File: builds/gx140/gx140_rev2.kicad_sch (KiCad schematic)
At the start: 14 parts

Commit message: Replace old GX140 drawings and PDFs with rev2 KiCad schematic
Co-Authored-By: Claude Sonnet 4.6 (1M context) <noreply@anthropic.com>
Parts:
- removed ? (x3): (no value), symbol grok:ANT
- removed ? (x4): (no value), symbol grok:MOTOR
- removed ?: (no value), symbol grok:RX
- removed ?: (no value), symbol grok:FC
- removed ?: (no value), symbol grok:VTX
- removed ?: (no value), symbol grok:BAT
- removed ?: (no value), symbol grok:ESC
- removed ?: (no value), symbol grok:GPS
- removed ?: (no value), symbol grok:CAM
- added AE1: SMA_Foxeer_Lollipop_RHCP, symbol grok:ANTENNA
- added AE2: ANT1_vert_L_standoff, symbol grok:ANTENNA
- added AE3: ANT2_horiz_top_plate, symbol grok:ANTENNA
- added BAT1: 2S_550mAh_LiHV_XT30, symbol grok:BATTERY_2S
- added CAM1: Caddx_Ant_1200TVL, symbol grok:CAM_CADDX_ANT
- added ESC1: BLS_35A_4in1_20x20_DShot600, symbol grok:ESC_BLS35A_4IN1
- added FC1: SpeedyBee_F405_Mini_20x20, symbol grok:FC_F405_MINI
- added GPS1: Matek_M10Q-5883_(opt), symbol grok:GPS_M10Q_5883
- added M1: Specter_1804_FL_CCW, symbol grok:MOTOR_1804
- added M2: Specter_1804_FR_CW, symbol grok:MOTOR_1804
- added M3: Specter_1804_RL_CCW, symbol grok:MOTOR_1804
- added M4: Specter_1804_RR_CW, symbol grok:MOTOR_1804
- added RX1: BETAFPV_SuperD_ELRS_Diversity, symbol grok:RX_SUPERD_ELRS
- added VTX1: HGLRC_Zeus_350mW_SmartAudio, symbol grok:VTX_ZEUS350
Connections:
- net 5V: now also CAM1.1 (5V), FC1.8 (5V), GPS1.1 (5V), RX1.1 (5V), VTX1.1 (5V)
- net CAM_VIDEO: now also CAM1.3 (VID), FC1.9 (VIN)
- net DSHOT_M1: now also ESC1.3 (S1), FC1.4 (M1)
- net DSHOT_M2: now also ESC1.4 (S2), FC1.5 (M2)
- net DSHOT_M3: now also ESC1.5 (S3), FC1.6 (M3)
- net DSHOT_M4: now also ESC1.6 (S4), FC1.7 (M4)
- net I2C_SCL: now also FC1.18 (SCL), GPS1.6 (SCL)
- net I2C_SDA: now also FC1.17 (SDA), GPS1.5 (SDA)
- net M1_A: now also ESC1.8 (M1_A), M1.1 (A)
- net M1_C: now also ESC1.10 (M1_C), M1.3 (C)
- net M2_A: now also ESC1.11 (M2_A), M2.1 (A)
- net M2_C: now also ESC1.13 (M2_C), M2.3 (C)
- net M3_A: now also ESC1.14 (M3_A), M3.1 (A)
- net M3_C: now also ESC1.16 (M3_C), M3.3 (C)
- net M4_A: now also ESC1.17 (M4_A), M4.1 (A)
- net M4_B: now also ESC1.18 (M4_B), M4.2 (B)
- net M4_C: now also ESC1.19 (M4_C), M4.3 (C)
- net RX_ANT1: now also AE2.1 (FEED), RX1.5 (ANT1)
- net RX_ANT2: now also AE3.1 (FEED), RX1.6 (ANT2)
- net VBAT: now also BAT1.1 (VBAT+), ESC1.1 (VBAT+), FC1.1 (VBAT)
- net VTX_ANT: now also AE1.1 (FEED), VTX1.5 (ANT)
- new net ESC_CURR: ESC1.7 (CURR), FC1.3 (CURR)
- new net GND: BAT1.2 (VBAT-), CAM1.2 (GND), ESC1.2 (VBAT-), FC1.2 (GND), GPS1.2 (GND), RX1.2 (GND), VTX1.2 (GND)
- new net M1_B: ESC1.9 (M1_B), M1.2 (B)
- new net M2_B: ESC1.12 (M2_B), M2.2 (B)
- new net M3_B: ESC1.15 (M3_B), M3.2 (B)
- new net RX3_GPS: FC1.16 (RX3), GPS1.4 (TX)
- new net RX5_CRSF: FC1.14 (RX5), RX1.4 (TX)
- new net TX3_GPS: FC1.15 (TX3), GPS1.3 (RX)
- new net TX4_SMARTAUDIO: FC1.11 (TX4), VTX1.4 (SA)
- new net TX5_CRSF: FC1.13 (TX5), RX1.3 (RX)
- new net VTX_VIDEO: FC1.10 (VOUT), VTX1.3 (VID_IN)
- no-connect marks 0 -> 1
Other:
- note added: "22AWG: VBAT, GND, motor phase | 26AWG: UART, DShot, video | 28AWG: I2C"
- note added: "=== UART MAP (F405 Mini) ==="
- note added: "=== VIDEO PATH (corrected) ==="
- note added: "=== WIRING ==="
- note added: "BAT XT30 -> ESC VBAT pads (22AWG). FC powered via ESC 8-pin harness (VBAT/GND/CURR/S1-S4)."
- note added: "CAM.VID -> FC.VIN (CAM_VIDEO) -> AT7456E OSD -> FC.VOUT -> VTX.VID_IN (VTX_VIDEO)."
- note added: "Continuity check VBAT-GND before battery | Verify motor order/direction in Betaflight Motors tab"
- note added: "FC internal 5V/3A BEC -> 5V net -> VTX, CAM, RX, GPS."
- note added: "GX140 3in ANALOG FPV — ELECTRICAL SCHEMATIC (Rev 2.0)"
- note added: "Grok rev1 bypassed the OSD: camera direct to VTX = no Betaflight OSD overlay."
- note added: "JST-SH 1.0mm: CAM | JST-GH 1.25mm: GPS | XT30: battery | Heat shrink all joints"
- note added: "METHOD: point-to-point by net label. Every conductor breaks out at the device pin."
- note added: "MOTOR PHASE WIRING: 3 conductors per motor (A/B/C)."
- note added: "Match net names to find the far end. No routed runs, no crossings, no junction ambiguity."
- note added: "Smoke stopper (ShortSaver) MANDATORY first power-up | Props OFF for motor direction test"
- note added: "Swap any two phases to reverse direction. M1 FL CCW | M2 FR CW | M3 RL CCW | M4 RR CW."
- note added: "UART3: GPS 57600 (TX3_GPS / RX3_GPS) | UART4: SmartAudio 2.1 (TX4 only, RX4 = N/C)"
- note added: "UART5: ELRS CRSF 420k (TX5_CRSF -> RX.RX, RX.TX -> RX5_CRSF) | I2C: QMC5883L compass"
- note removed: "2S 550mAh LiHV (7.4V) XT30 → FC VBAT → Internal 5V/3A BEC → 5V Rail"
- note removed: "2S 550mAh LiHV 7.4V XT30"
- note removed: "5V Rail powers: VTX, CAM, RX, GPS (optional)"
- note removed: "5V: FC1.5V → VTX1.5V → CAM1.5V → RX1.5V → GPS1.5V"
- note removed: "=== BUILD SPECS ==="
- note removed: "=== NET CROSS-REFERENCE ==="
- note removed: "=== SIGNAL SUMMARY ==="
- note removed: "BAT1"
- note removed: "BAT: 2S 550mAh LiHV 7.6V 75C XT30 30×18×15mm ~4-5min LVC 3.5V/cell"
- note removed: "BETAFPV SuperD ELRS V3 22x14mm Dual SX1280"
- note removed: "BLS 35A 4in1 20x20 DShot600 3-6S"
- note removed: "CAM Video → VTX CAM_IN (JST-SH 1.0mm 4-pin)"
- note removed: "CAM1"
- note removed: "CAM: Caddx Ant 1200TVL 14×14→19×19 adapter F1.6 165° JST-SH 1.0mm 4-pin"
- note removed: "CAM_VIDEO: CAM1.CAM_VIDEO → VTX1.CAM_VIDEO (JST-SH 1.0mm)"
- note removed: "CURR: ESC1.CURR → FC1.CURR (current sense, if supported)"
- note removed: "Caddx Ant 1200TVL 14x14→19x19 F1.6 JST-SH"
- note removed: "Continuity check all rails | AUW ~190g (<250g) | CG <1mm | ALL DIRECT FIT"
- note removed: "DSHOT_M1-M4: FC1.M1-M4 → ESC1.DSHOT_M1-M4 (DShot600)"
- note removed: "DShot600: FC M1-M4 → ESC → Motors (bidirectional, RPM filter ON)"
- note removed: "ESC1"
- note removed: "ESC: BLS 35A 4in1 20×20 DShot600 Bidir ON | 25×25×4.5mm | 3-6S | 5V/3A BEC"
- note removed: "FC1"
- note removed: "FC: SpeedyBee F405 Mini 20×20 ICM42688 DPS310 | 25×25×6.5mm | 4 UARTs USB-C"
- note removed: "Frame: GX140 140mm 4mm CF twin 20x20 | 8× M3×25mm alu standoffs | ~45g bare"
- note removed: "GND: BAT1.GND → ESC1.GND → FC1.GND → VTX1.GND → CAM1.GND → RX1.GND → GPS1.GND"
- note removed: "GPS1"
- note removed: "GPS: Matek M10Q-5883 UBLOX M10 QMC5883L (optional) JST-GH 1.25mm 6-pin"
- note removed: "GROK — FPV Drone Engineering | 2025-12-12 | Rev 2.0 | Sheet 1/1 | A3"
- note removed: "GX140 3in ANALOG FPV — Electrical Schematic"
- note removed: "HGLRC Specter 1804 3500KV M1 FL CCW"
- note removed: "HGLRC Specter 1804 3500KV M2 FR CW"
- note removed: "HGLRC Specter 1804 3500KV M3 RL CCW"
- note removed: "HGLRC Specter 1804 3500KV M4 RR CW"
- note removed: "HGLRC Zeus 350mW 16x16→20x20 SmartAudio"
- note removed: "I2C_SDA/SCL: FC1.I2C → GPS1.I2C (QMC5883L compass)"
- note removed: "M1"
- note removed: "M1_A-M4_C: ESC1.M1_A-M4_C → M1-M4 (Motor phases)"
- note removed: "M2"
- note removed: "M3"
- note removed: "M4"
- note removed: "Matek M10Q-5883 UBLOX M10 QMC5883L (optional)"
- note removed: "Motors: HGLRC Specter 1804 3500KV 13.3g 12×12 M2 1.5mm shaft 22.68×13.2mm"
- note removed: "Props: GEMFAN 3052 3in tri-blade 5mm hub+1.5mm adapter 22.8mm tip clearance"
- note removed: "RX1"
- note removed: "RX3/TX3: FC1.RX3 → GPS1.TX3 | FC1.TX3 → GPS1.RX3 (UBLOX)"
- note removed: "RX: BETAFPV SuperD ELRS 22×14mm 1.1g Dual SX1280 CRSF@420k ANT1 vert L ANT2 horiz"
- note removed: "SMA → Foxeer Lollipop RHCP"
- note removed: "ShortSaver MANDATORY before first power | Props OFF for motor direction test"
- note removed: "SpeedyBee F405 Mini 20x20 ICM42688 DPS310 4 UARTs"
- note removed: "TX4: FC1.TX4 → VTX1.TX4 (SmartAudio PA control)"
- note removed: "TX5/RX5: FC1.TX5 → RX1.RX5 | RX1.TX5 → FC1.RX5 (CRSF)"
- note removed: "UART3 (TX3/RX3): FC ↔ GPS UBLOX — M10Q-5883, 57600 baud (optional)"
- note removed: "UART4 (TX4): FC → VTX SmartAudio RX — PA control, 115200 baud"
- note removed: "UART5 (TX5/RX5): FC ↔ RX CRSF — ELRS V3, 420000 baud"
- note removed: "VBAT: BAT1.VBAT → ESC1.VBAT → FC1.VBAT"
- note removed: "VTX1"
- note removed: "VTX: HGLRC Zeus 350mW 16×16→20×20 SmartAudio SMA Foxeer Lollipop RHCP"
- company: GROK — FPV Drone Engineering -> GX140 Build — net-label point-to-point method

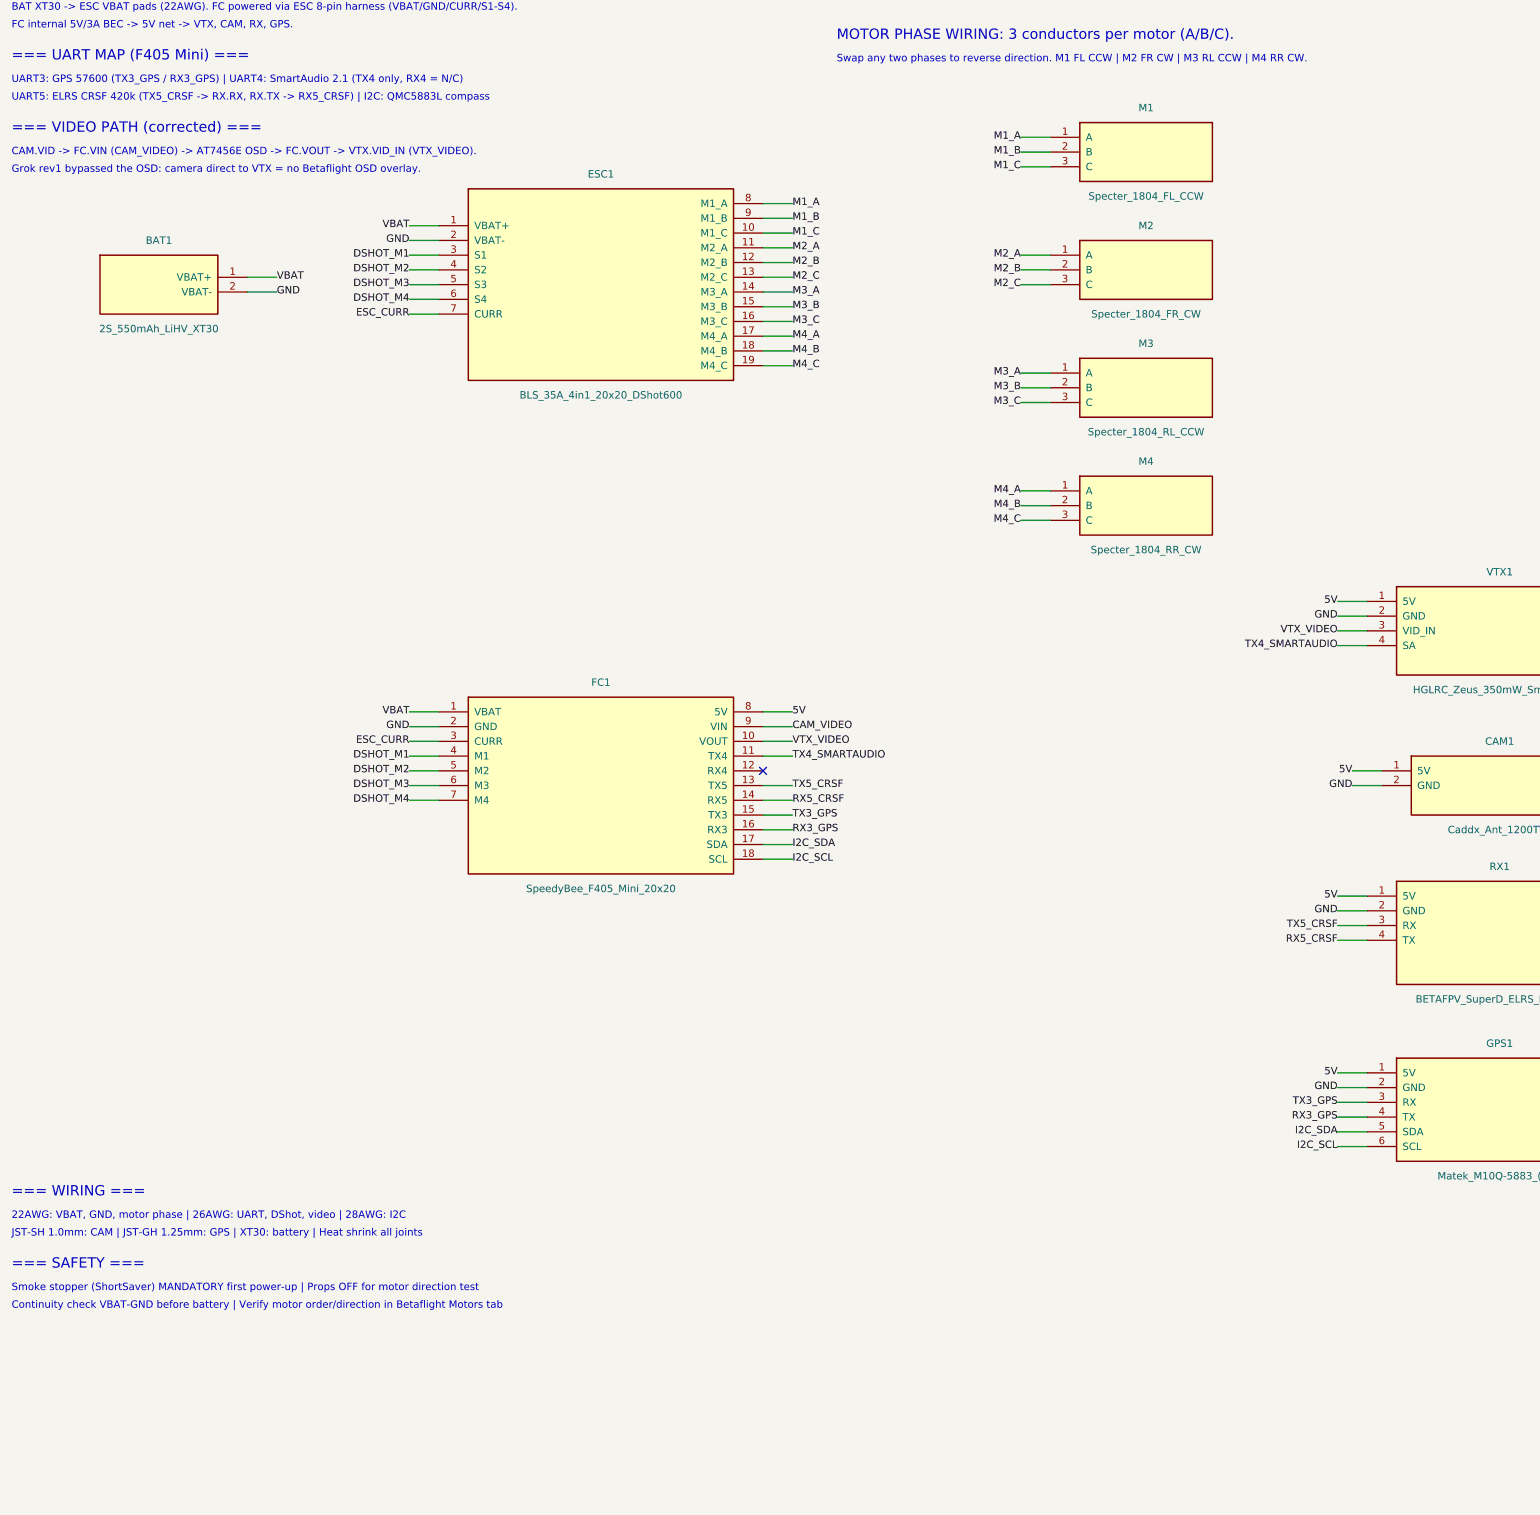
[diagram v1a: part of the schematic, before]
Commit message: Add engineering package text annotations to KiCad schematic
Full wire schedule, reverse wire tagging method, stack assembly
layers, torque specs, mounting notes, antenna layout, battery
info, and Betaflight config — all in-schematic annotations.

Co-Authored-By: Claude Sonnet 4.6 (1M context) <noreply@anthropic.com>
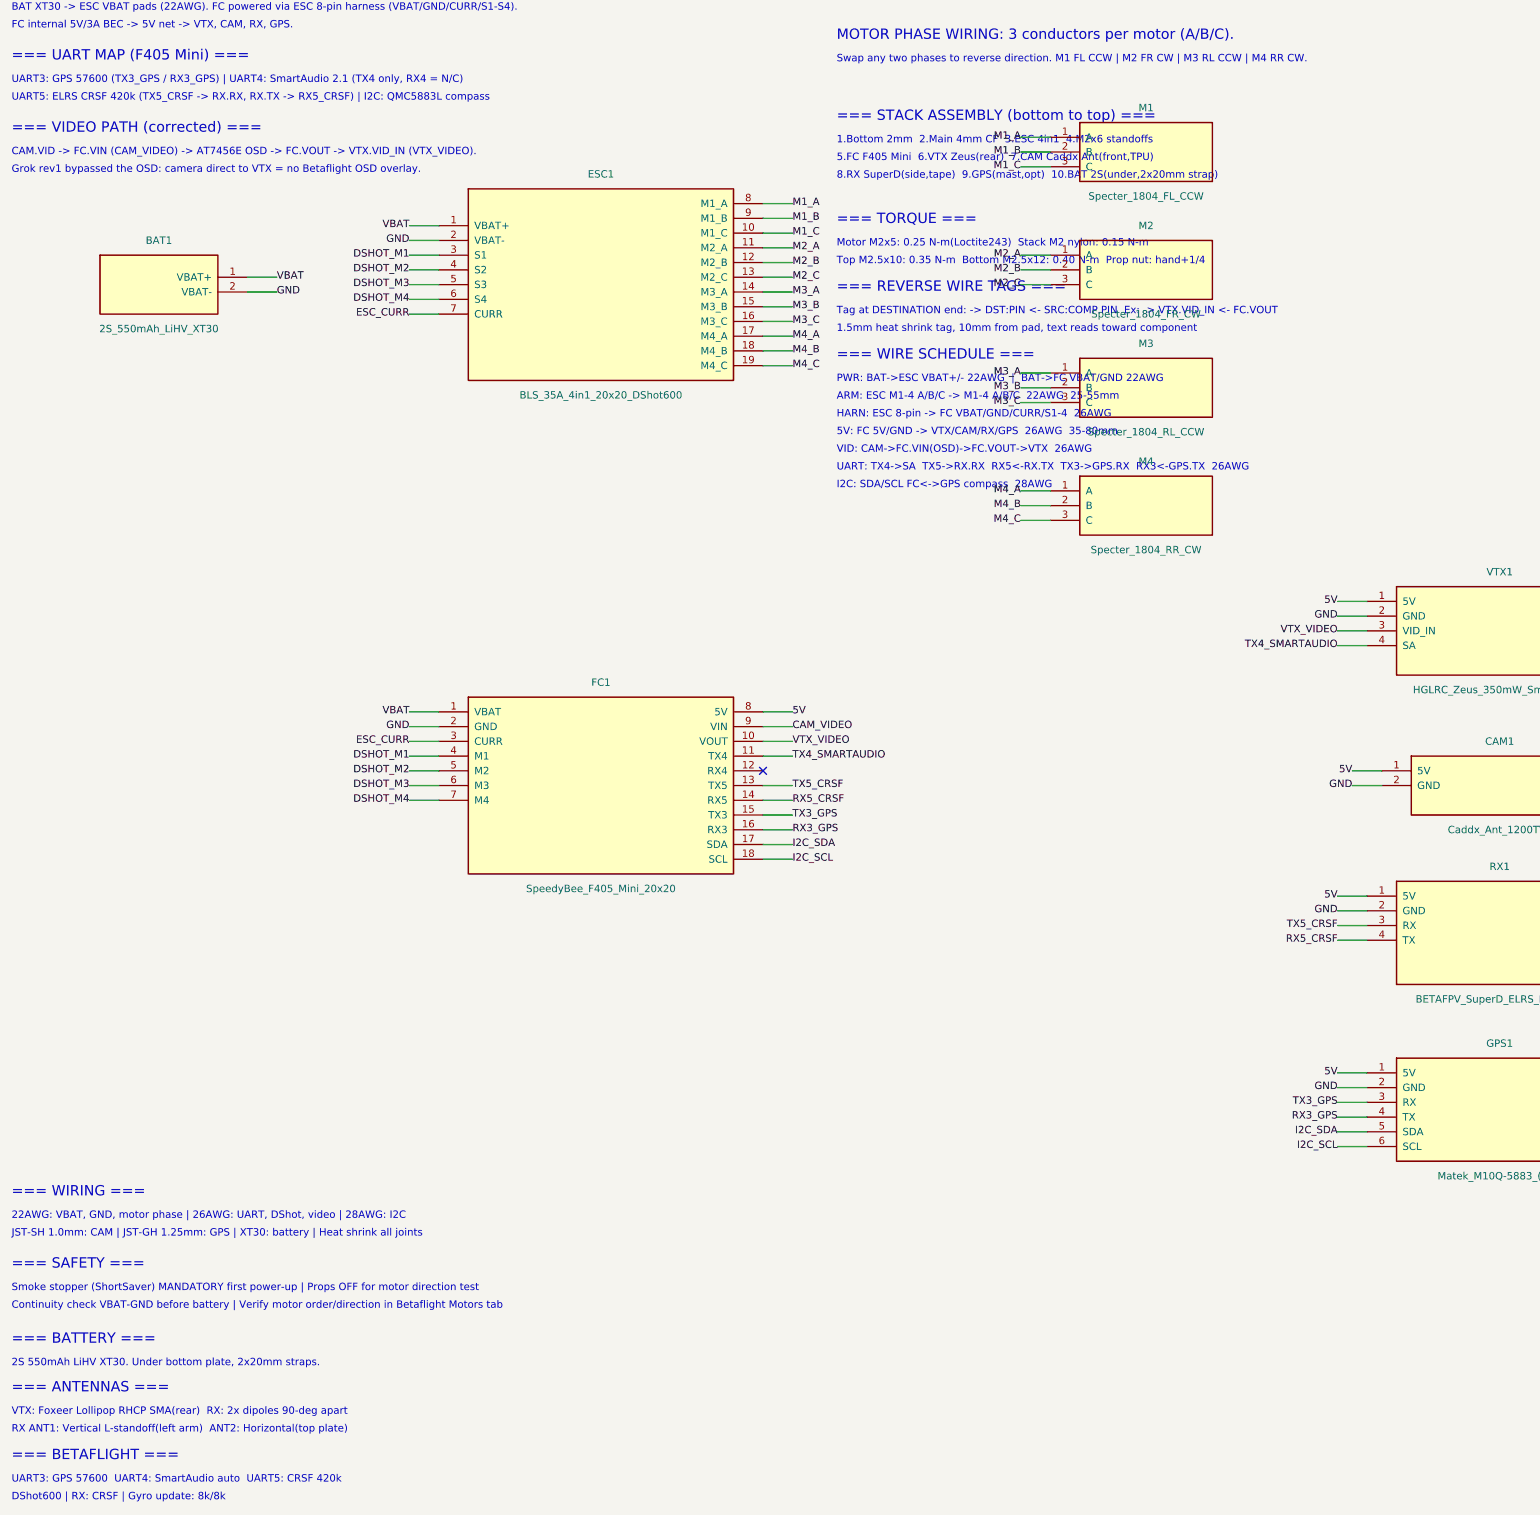
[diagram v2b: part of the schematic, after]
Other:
- note added: "1.5mm heat shrink tag, 10mm from pad, text reads toward component"
- note added: "1.Bottom 2mm 2.Main 4mm CF 3.ESC 4in1 4.M2x6 standoffs"
- note added: "2S 550mAh LiHV XT30. Under bottom plate, 2x20mm straps."
- note added: "5.FC F405 Mini 6.VTX Zeus(rear) 7.CAM Caddx Ant(front,TPU)"
- note added: "5V: FC 5V/GND -> VTX/CAM/RX/GPS 26AWG 35-80mm"
- note added: "8.RX SuperD(side,tape) 9.GPS(mast,opt) 10.BAT 2S(under,2x20mm strap)"
- note added: "=== ANTENNAS ==="
- note added: "=== BATTERY ==="
- note added: "=== BETAFLIGHT ==="
- note added: "=== REVERSE WIRE TAGS ==="
- note added: "=== STACK ASSEMBLY (bottom to top) ==="
- note added: "=== TORQUE ==="
- note added: "=== WIRE SCHEDULE ==="
- note added: "ARM: ESC M1-4 A/B/C -> M1-4 A/B/C 22AWG 25-55mm"
- note added: "DShot600 | RX: CRSF | Gyro update: 8k/8k"
- note added: "HARN: ESC 8-pin -> FC VBAT/GND/CURR/S1-4 26AWG"
- note added: "I2C: SDA/SCL FC<->GPS compass 28AWG"
- note added: "Motor M2x5: 0.25 N-m(Loctite243) Stack M2 nylon: 0.15 N-m"
- note added: "PWR: BAT->ESC VBAT+/- 22AWG | BAT->FC VBAT/GND 22AWG"
- note added: "RX ANT1: Vertical L-standoff(left arm) ANT2: Horizontal(top plate)"
- note added: "Tag at DESTINATION end: -> DST:PIN <- SRC:COMP.PIN Ex: -> VTX.VID_IN <- FC.VOUT"
- note added: "Top M2.5x10: 0.35 N-m Bottom M2.5x12: 0.40 N-m Prop nut: hand+1/4"
- note added: "UART3: GPS 57600 UART4: SmartAudio auto UART5: CRSF 420k"
- note added: "UART: TX4->SA TX5->RX.RX RX5<-RX.TX TX3->GPS.RX RX3<-GPS.TX 26AWG"
- note added: "VID: CAM->FC.VIN(OSD)->FC.VOUT->VTX 26AWG"
- note added: "VTX: Foxeer Lollipop RHCP SMA(rear) RX: 2x dipoles 90-deg apart"
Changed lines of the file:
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@@
+    (effects (font (size 1.27 1.27)) (justify left bottom))
+  )
+  (text "=== STACK ASSEMBLY (bottom to top) ===" (at 167.64 60.96 0)
+    (effects (font (size 1.778 1.778)) (justify left bottom))
+  )
+  (text "1.Bottom 2mm  2.Main 4mm CF  3.ESC 4in1  4.M2x6 standoffs" (at 167.64 64.77 0)
+    (effects (font (size 1.27 1.27)) (justify left bottom))
+  )
+  (text "5.FC F405 Mini  6.VTX Zeus(rear)  7.CAM Caddx Ant(front,TPU)" (at 167.64 67.82 0)
+    (effects (font (size 1.27 1.27)) (justify left bottom))
+  )
+  (text "8.RX SuperD(side,tape)  9.GPS(mast,opt)  10.BAT 2S(under,2x20mm strap)" (at 167.64 70.87 0)
+    (effects (font (size 1.27 1.27)) (justify left bottom))
+  )
+  (text "=== TORQUE ===" (at 167.64 78.74 0)
+    (effects (font (size 1.778 1.778)) (justify left bottom))
+  )
+  (text "Motor M2x5: 0.25 N-m(Loctite243)  Stack M2 nylon: 0.15 N-m" (at 167.64 82.55 0)
+    (effects (font (size 1.27 1.27)) (justify left bottom))
+  )
+  (text "Top M2.5x10: 0.35 N-m  Bottom M2.5x12: 0.40 N-m  Prop nut: hand+1/4" (at 167.64 85.6 0)
+    (effects (font (size 1.27 1.27)) (justify left bottom))
+  )
+  (text "=== REVERSE WIRE TAGS ===" (at 167.64 90.42 0)
+    (effects (font (size 1.778 1.778)) (justify left bottom))
+  )
+  (text "Tag at DESTINATION end: -> DST:PIN <- SRC:COMP.PIN  Ex: -> VTX.VID_IN <- FC.VOUT" (at 167.64 94.23 0)
+    (effects (font (size 1.27 1.27)) (justify left bottom))
+  )
+  (text "1.5mm heat shrink tag, 10mm from pad, text reads toward component" (at 167.64 97.28 0)
+    (effects (font (size 1.27 1.27)) (justify left bottom))
+  )
+  (text "=== WIRE SCHEDULE ===" (at 167.64 102.11 0)
+    (effects (font (size 1.778 1.778)) (justify left bottom))
+  )
+  (text "PWR: BAT->ESC VBAT+/- 22AWG  |  BAT->FC VBAT/GND 22AWG" (at 167.64 105.92 0)
+    (effects (font (size 1.27 1.27)) (justify left bottom))
+  )
+  (text "ARM: ESC M1-4 A/B/C -> M1-4 A/B/C  22AWG  25-55mm" (at 167.64 108.97 0)
+    (effects (font (size 1.27 1.27)) (justify left bottom))
+  )
+  (text "HARN: ESC 8-pin -> FC VBAT/GND/CURR/S1-4  26AWG" (at 167.64 112.02 0)
+    (effects (font (size 1.27 1.27)) (justify left bottom))
+  )
+  (text "5V: FC 5V/GND -> VTX/CAM/RX/GPS  26AWG  35-80mm" (at 167.64 115.07 0)
+    (effects (font (size 1.27 1.27)) (justify left bottom))
+  )
+  (text "VID: CAM->FC.VIN(OSD)->FC.VOUT->VTX  26AWG" (at 167.64 118.12 0)
+    (effects (font (size 1.27 1.27)) (justify left bottom))
+  )
+  (text "UART: TX4->SA  TX5->RX.RX  RX5<-RX.TX  TX3->GPS.RX  RX3<-GPS.TX  26AWG" (at 167.64 121.17 0)
+    (effects (font (size 1.27 1.27)) (justify left bottom))
+  )
+  (text "I2C: SDA/SCL FC<->GPS compass  28AWG" (at 167.64 124.22 0)
+    (effects (font (size 1.27 1.27)) (justify left bottom))
+  )
+  (text "=== BATTERY ===" (at 25.4 271.78 0)
+    (effects (font (size 1.778 1.778)) (justify left bottom))
+  )
+  (text "2S 550mAh LiHV XT30. Under bottom plate, 2x20mm straps." (at 25.4 275.59 0)
+    (effects (font (size 1.27 1.27)) (justify left bottom))
+  )
+  (text "=== ANTENNAS ===" (at 25.4 280.16 0)
+    (effects (font (size 1.778 1.778)) (justify left bottom))
+  )
+  (text "VTX: Foxeer Lollipop RHCP SMA(rear)  RX: 2x dipoles 90-deg apart" (at 25.4 283.97 0)
+    (effects (font (size 1.27 1.27)) (justify left bottom))
+  )
+  (text "RX ANT1: Vertical L-standoff(left arm)  ANT2: Horizontal(top plate)" (at 25.4 287.02 0)
+    (effects (font (size 1.27 1.27)) (justify left bottom))
+  )
+  (text "=== BETAFLIGHT ===" (at 25.4 291.84 0)
+    (effects (font (size 1.778 1.778)) (justify left bottom))
+  )
+  (text "UART3: GPS 57600  UART4: SmartAudio auto  UART5: CRSF 420k" (at 25.4 295.65 0)
+    (effects (font (size 1.27 1.27)) (justify left bottom))
+  )
+  (text "DShot600 | RX: CRSF | Gyro update: 8k/8k" (at 25.4 298.7 0)
     (effects (font (size 1.27 1.27)) (justify left bottom))
   )
